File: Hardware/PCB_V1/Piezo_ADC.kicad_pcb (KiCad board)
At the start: 2 copper layers, 165 x 44.2 mm, 51 parts, among them J1 Conn_RJ45_Shielded_8p8c_RA_A-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, J2 Conn_2Pos_3.96mm_1Row_TH_JST_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, U1 IC_LDO_FIXED_3.3V_SC-70-5, U2 IC_TRANSCIEVER_RS485_DUPLEX_S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, U3 IC_ADC_SPI_12BIT_ADC121S021_S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, U4 IC_OPAMP_1MHz_TLV9001IDBVR_1A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, U5 IC_TRANSCIEVER_RS485_DUPLEX_S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

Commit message: Converted Altium PCB File to KiCAD
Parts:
- added TP6: TPAD6R, Footprints-lib:Single_TH_Pin_Header, F.Cu at (169.8, 105.4)
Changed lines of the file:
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@@
 		)
+	)
+	(footprint "Footprints-lib:Single_TH_Pin_Header"
+		(layer "F.Cu")
+		(at 169.782885 105.43992)
+		(property "Reference" "TP6"
+			(at 0 -2.54 0)
+			(unlocked yes)
+			(layer "F.SilkS")
+			(effects
+				(font
+					(size 1 1)
+					(thickness 0.1)
+				)
+			)
+		)
+		(property "Value" "TPAD6R"
+			(at 0 2.54 0)
+			(unlocked yes)
+			(layer "F.Fab")
+			(effects
+				(font
+					(size 1 1)
+					(thickness 0.15)
+				)
+			)
+		)
+		(property "Datasheet" ""
+			(at 0 0 0)
+			(unlocked yes)
+			(layer "F.Fab")
+			(hide yes)
+			(effects
+				(font
+					(size 1 1)
+					(thickness 0.15)
+				)
+			)
+		)
+		(property "Description" "0.6mm round"
+			(at 0 0 0)
+			(unlocked yes)
+			(layer "F.Fab")
+			(hide yes)
+			(effects
+				(font
+					(size 1 1)
+					(thickness 0.15)
+				)
+			)
+		)
+		(property "CASE/PACKAGE" ""
+			(at 0 0 0)
+			(unlocked yes)
+			(layer "F.Fab")
+			(hide yes)
+			(effects
+				(font
+					(size 1 1)
+					(thickness 0.15)
+				)
+			)
+		)
+		(property "ROHS COMPLIANT" ""
+			(at 0 0 0)
+			(unlocked yes)
+			(layer "F.Fab")
+			(hide yes)
+			(effects
+				(font
+					(size 1 1)
+					(thickness 0.15)
+				)
+			)
+		)
+		(property "MAX OPERATING TEMPERATURE" ""
+			(at 0 0 0)
+			(unlocked yes)
+			(layer "F.Fab")
+			(hide yes)
+			(effects
+				(font
+					(size 1 1)
+					(thickness 0.15)
+				)
+			)
+		)
+		(property "MIN OPERATING TEMPERATURE" ""
+			(at 0 0 0)
+			(unlocked yes)
+			(layer "F.Fab")
+			(hide yes)
+			(effects
+				(font
+					(size 1 1)
+					(thickness 0.15)
+				)
+			)
+		)
+		(property "MOUNTING TECHNOLOGY" ""
+			(at 0 0 0)
+			(unlocked yes)
+			(layer "F.Fab")
+			(hide yes)
+			(effects
+				(font
+					(size 1 1)
+					(thickness 0.15)
+				)
+			)
+		)
+		(property "PINS" "1"
+			(at 0 0 0)
+			(unlocked yes)
+			(layer "F.Fab")
+			(hide yes)
+			(effects
+				(font
+					(size 1 1)
+					(thickness 0.15)
+				)
+			)
+		)
+		(property ki_fp_filters "*TP06R*")
+		(sheetname "/")
+		(sheetfile "Piezo_ADC.kicad_sch")
+		(units
+			(unit
+				(name "A")
+				(pins "1")
+			)
+		)
+		(attr board_only)
+		(duplicate_pad_numbers_are_jumpers no)
+		(fp_circle
+			(center 0 0)
+			(end 1 0)
+			(stroke
+				(width 0.1)
+				(type solid)
+			)
+			(fill no)
+			(layer "F.SilkS")
+		)
+		(fp_rect
+			(start -1.52 -1.52)
+			(end 1.52 1.52)
+			(stroke
+				(width 0.05)
+				(type default)
+			)
+			(fill no)
+			(layer "F.CrtYd")
+		)
+		(fp_rect
+			(start -1.27 -1.27)
+			(end 1.27 1.27)
+			(stroke
+				(width 0.1)
+				(type default)
+			)
+			(fill no)
+			(layer "F.Fab")
+		)
+		(fp_text user "${REFERENCE}"
+			(at 0 3.81 0)
+			(unlocked yes)
+			(layer "F.Fab")
+			(effects
+				(font
+					(size 1 1)
+					(thickness 0.15)
+				)
+			)
+		)
+		(pad "1" thru_hole circle
+			(at 0 0)
+			(size 1.5 1.5)
+			(drill 0.8)
+			(layers "*.Cu" "*.Mask")
+			(remove_unused_layers no)
+			(net "/CS_SE")
+			(pinfunction "TP_1")
+			(pintype "passive")
+		)
+		(embedded_fonts no)
 	)
 	(footprint "Vault:RES_0402"

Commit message: Added 5015 test points to schematic
Waiting to get confirmation before I place them on the board.
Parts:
- added TP7: TPAD6R, TestPoint:TestPoint_Keystone_5015_Micro_Mini, F.Cu at (169.8, 108.9)
- added TP8: TPAD6R, TestPoint:TestPoint_Keystone_5015_Micro_Mini, F.Cu at (169.8, 115.2)
- TP6: footprint Footprints-lib:Single_TH_Pin_Header -> TestPoint:TestPoint_Keystone_5015_Micro_Mini
- moved TP6 2.75 mm to (169.8, 102.7)

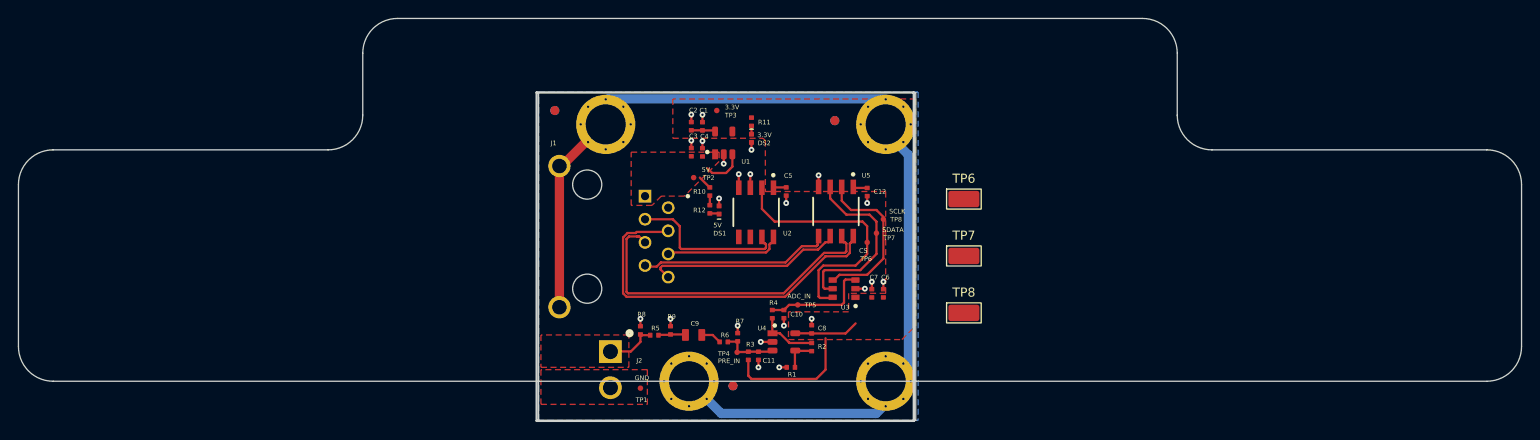
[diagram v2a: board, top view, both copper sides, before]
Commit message: PCB Updates
- Added keystone 5001 test points
- Added Schottky diodes
- reworked the board layout to make room for TPs and additional components.
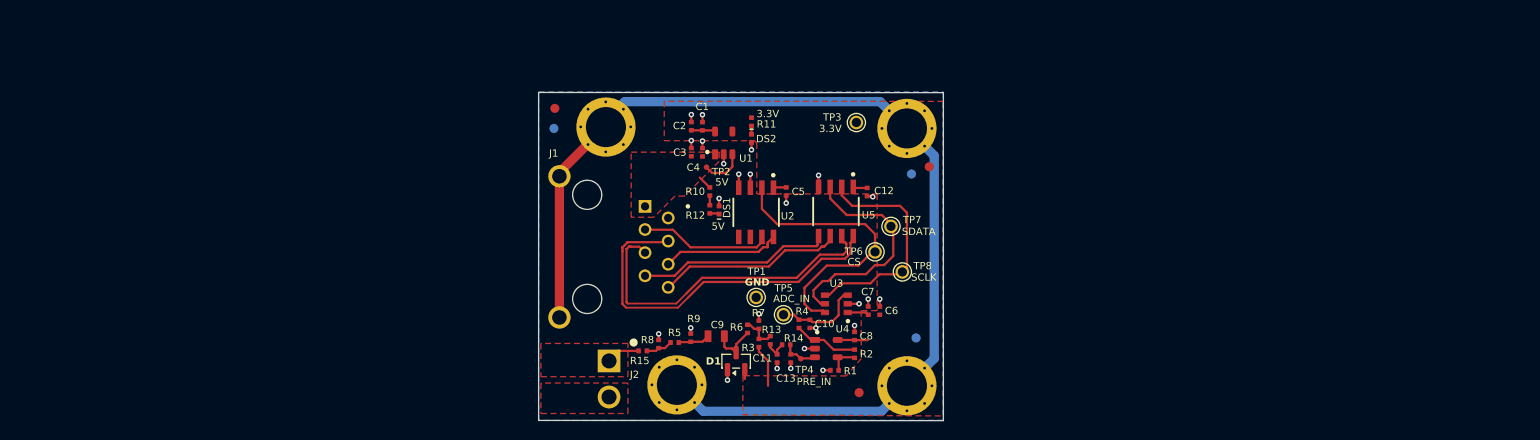
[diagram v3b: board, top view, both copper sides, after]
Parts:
- removed the TP6 at (169.8, 102.7)
- removed the TP6 at (159.2, 107.5)
- removed the TP7 at (169.8, 108.9)
- removed the TP7 at (160.2, 106.4)
- removed the TP8 at (169.8, 115.2)
- removed the TP8 at (160.9, 104.9)
- added C13: Cap_0.1uF_10%_16V_0402, Piezo_Footprints:CAP_0402_0.6mm_Height, F.Cu at (150.8, 120.2)
- added D1: BAT54S, Package_TO_SOT_SMD:SOT-23, F.Cu at (144.8, 120.5)
- added R13: Res_0R0_1%_63mW_0402, Piezo_Footprints:RES_0402, F.Cu at (148.5, 118.2)
- added R14: Res_0R0_1%_63mW_0402, Piezo_Footprints:RES_0402, F.Cu at (150.3, 118.7)
- added R15: Res_0R0_1%_63mW_0402, Piezo_Footprints:RES_0402, F.Cu at (134.5, 119.4)
- added TP6: TPAD6R, Piezo_Footprints:Keystone 5001 TP, F.Cu at (160.0, 108.5)
- added TP7: TPAD6R, Piezo_Footprints:Keystone 5001 TP, F.Cu at (161.8, 105.7)
- added TP8: TPAD6R, Piezo_Footprints:Keystone 5001 TP, F.Cu at (163.0, 110.7)
- C1, C10, C11, C12, C2, C3, C4, C5, C6, C7, C8: footprint Vault:CAP_0402_0.6mm_Height -> Piezo_Footprints:CAP_0402_0.6mm_Height
- C9: footprint Vault:CAP_0805_1.45mm_Height -> Piezo_Footprints:CAP_0805_1.45mm_Height
- DS1, DS2: footprint Vault:LED_0402_Green_KA -> Piezo_Footprints:LED_0402_Green_KA
- FD1, FD3, FD5, FD6: footprint Vault:FID1X2R -> Piezo_Footprints:FID1X2R
- FD2: footprint Vault:FID1X2R -> Piezo_Footprints:FID1X2R; moved to B.Cu
- FD4: footprint Vault:FID1X2R -> Piezo_Footprints:FID1X2R; moved to F.Cu
- J1: footprint Vault:A-2004-2-4-LPS-N-R -> Piezo_Footprints:A-2004-2-4-LPS-N-R
- J2: footprint Vault:JST_B2PS-VH-FP -> Piezo_Footprints:JST_B2PS-VH-FP
- MP1, MP2, MP3, MP4: footprint Vault:9774020960 -> Piezo_Footprints:9774020960
- R1, R10, R11, R12, R2, R3, R4, R5, R6, R7, R8, R9: footprint Vault:RES_0402 -> Piezo_Footprints:RES_0402
- TP1, TP3, TP5: footprint Vault:TP06R -> Piezo_Footprints:Keystone 5001 TP
- TP2, TP4: footprint Vault:TP06R -> Piezo_Footprints:TP06R
- U1, U4: footprint Vault:SOT23-5 -> Piezo_Footprints:SOT23-5
- U2, U5: footprint Vault:SOIC-8 -> Piezo_Footprints:SOIC-8
- U3: footprint Vault:SOT-23-6 -> Piezo_Footprints:SOT-23-6
- moved FD4 45.6 mm to (158.3, 123.9), turned to 0 degrees
- moved FD3 32.3 mm to (166.0, 99.1), turned to 0 degrees
- moved FD5 30.8 mm to (124.8, 94.9), turned to 180 degrees
- moved FD6 30.4 mm to (164.0, 99.9), turned to 180 degrees
- moved FD2 25.5 mm to (164.5, 117.9), turned to 180 degrees
- moved TP1 16.1 mm to (147.0, 113.5)
- moved TP3 15.4 mm to (158.0, 94.3), turned to 0 degrees
- moved TP4 7.03 mm to (151.9, 120.2)
- moved R1 4.81 mm to (155.6, 121.5)
- moved C8 4.77 mm to (157.8, 117.7)
- moved R2 4.77 mm to (157.8, 119.7)
- moved U4 4.71 mm to (154.7, 119.1)
- moved R4 3.12 mm to (151.7, 116.4)
- moved C10 3.05 mm to (152.9, 116.4)
- moved R6 2.98 mm to (146.0, 116.9), turned to 90 degrees
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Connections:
- net ADC_IN renamed /ADC_IN
- net CS_DIFF_N renamed /CS_DIFF_N
- net CS_DIFF_P renamed /CS_DIFF_P
- net NetC9_1 renamed Net-(C9-Pad1)
- net NetC9_2 renamed Net-(D1-COM)
- net NetDS1_1 renamed Net-(DS1-A)
- net NetDS2_1 renamed Net-(DS2-A)
- net NetR10_1 renamed Net-(R10-Pad1)
- net NetR1_1 renamed Net-(U4--IN)
- net NetR2_2 renamed Net-(U4-OUT)
- net SCLK_DIFF_N renamed /SCLK_DIFF_N
- net SCLK_DIFF_P renamed /SCLK_DIFF_P
- net SDATA_DIFF_N renamed /SDATA_DIFF_N
- net SDATA_DIFF_P renamed /SDATA_DIFF_P
- C11 pad 1: PREAMP_IN -> Net-(C11-Pad1)
- J2 pad 1: PIEZO_IN -> /PIEZO_IN
- R3 pad 1: PREAMP_IN -> Net-(R13-Pad1)
- R5 pad 1: PIEZO_IN -> Net-(R15-Pad2)
- R6 pad 2: PREAMP_IN -> Net-(R13-Pad1)
- R7 pad 2: PREAMP_IN -> Net-(R13-Pad1)
- R8 pad 2: PIEZO_IN -> Net-(R15-Pad2)
- TP4 pad 1: PREAMP_IN -> /PREAMP_IN
- U1 pad 4: (no net) -> unconnected-(U1-NC-Pad4)
- U2 pad 2: CS_SE -> /CS_SE
- U2 pad 5: (no net) -> unconnected-(U2-Y-Pad5)
- U2 pad 6: (no net) -> unconnected-(U2-Z-Pad6)
- U3 pad 4: SCLK_SE -> /SCLK_SE
- U3 pad 5: SDATA_SE -> /SDATA_SE
- U3 pad 6: CS_SE -> /CS_SE
- U4 pad 3: PREAMP_IN -> /PREAMP_IN
- U5 pad 2: SCLK_SE -> /SCLK_SE
- U5 pad 3: SDATA_SE -> /SDATA_SE
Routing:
- net /CS_SE: track 0.00 -> 31.4 mm
- net CS_SE: track 28.2 -> 0.00 mm
- net /SDATA_SE: track 0.00 -> 25.3 mm
- net /SCLK_SE: track 0.00 -> 25.1 mm
- net SDATA_SE: track 20.4 -> 0.00 mm
- net SCLK_SE: track 17.5 -> 0.00 mm
- net 3V3: track 27.0 -> 16.5 mm
- net PREAMP_IN: track 6.30 -> 0.00 mm
- net CH_GND: track 114.1 -> 120.3 mm
- net PIEZO_IN: track 5.67 -> 0.00 mm
- net Net-(R13-Pad1): track 0.00 -> 3.91 mm
- net /PREAMP_IN: track 0.00 -> 3.75 mm
- net /PIEZO_IN: track 0.00 -> 3.73 mm
- net Net-(D1-COM): track 2.28 -> 5.91 mm
- net Net-(R15-Pad2): track 0.00 -> 2.98 mm
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- added copper zone on F.Cu, net /PIEZO_IN
- removed copper zone on F.Cu, net PIEZO_IN
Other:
- board size 165 x 44.2 mm -> 44.4 x 36 mm

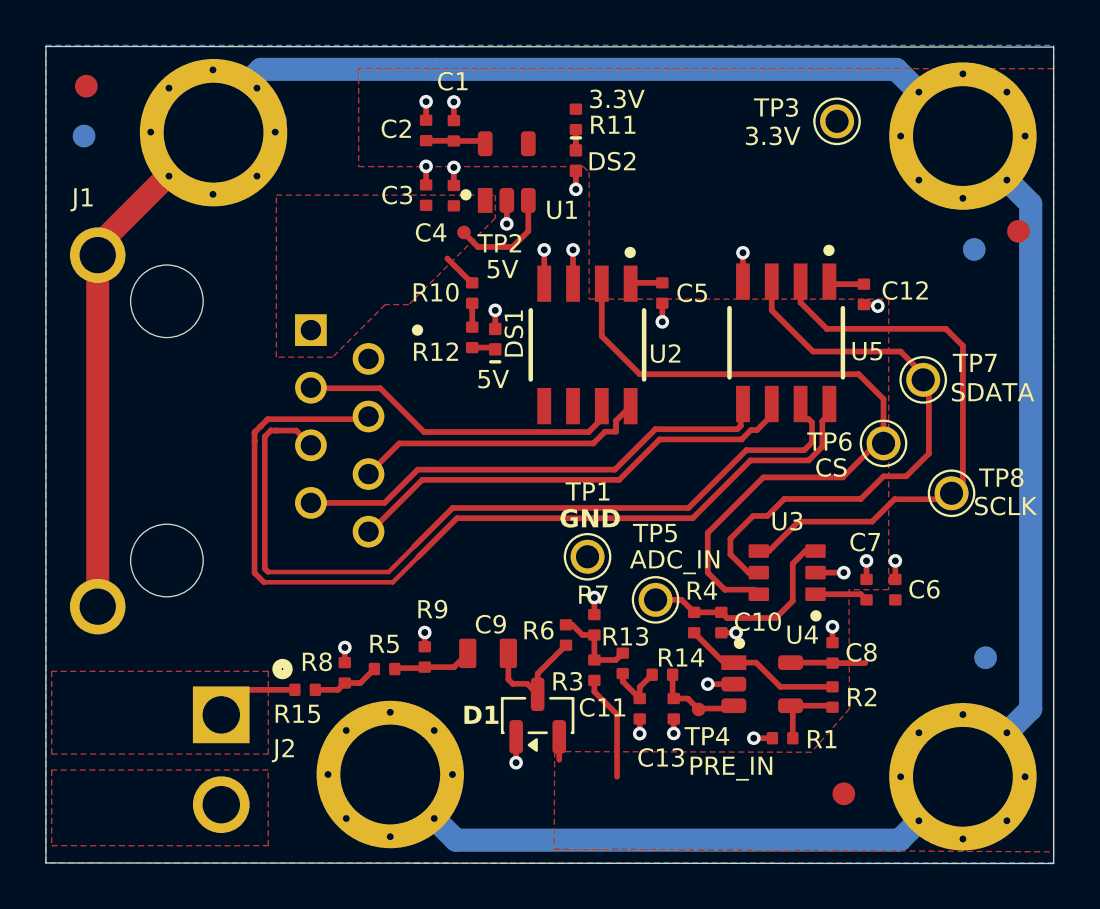
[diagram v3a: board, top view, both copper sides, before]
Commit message: Moved fiducial markers, removed section of solder mask from risers we are no longer using.
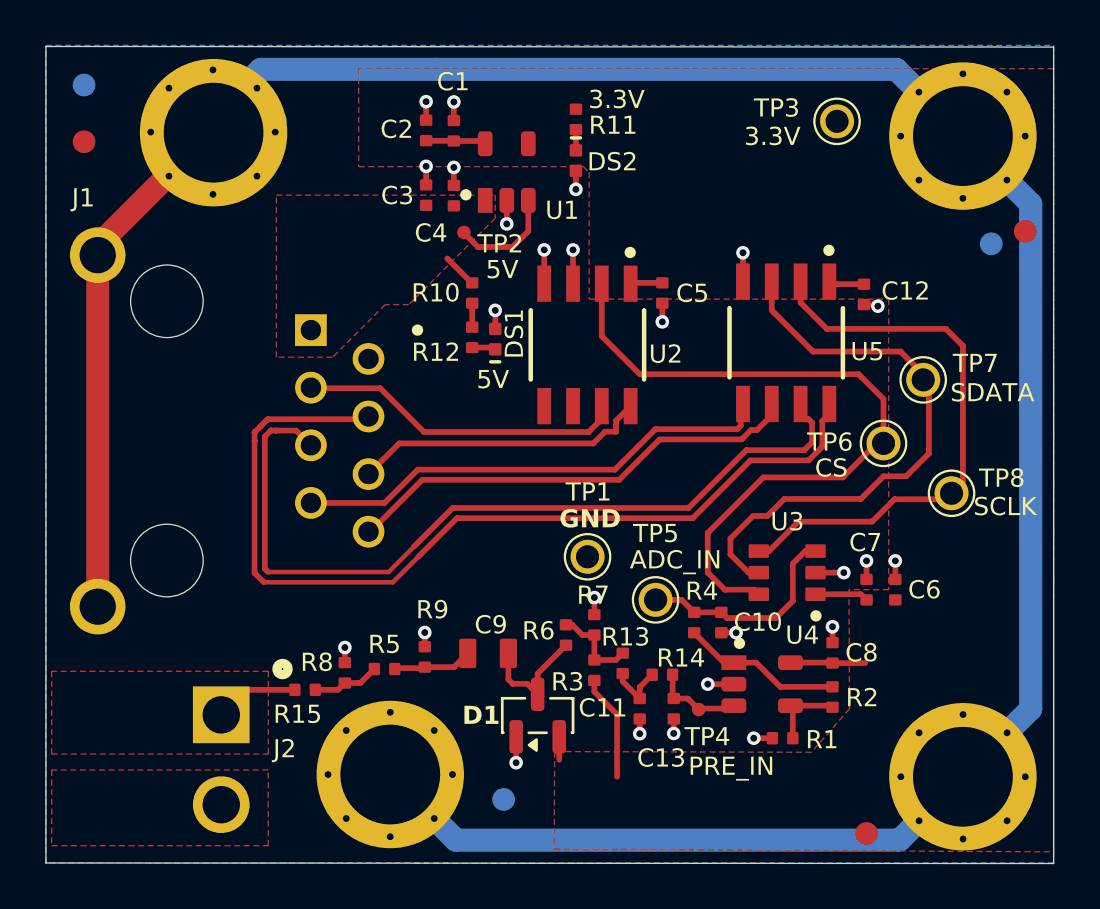
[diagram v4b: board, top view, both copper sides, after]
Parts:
- C11: value Cap_0.1uF_10%_16V_0402 -> Cap_2.05nF_10%_16V_0402
- C13: value Cap_0.1uF_10%_16V_0402 -> Cap_1nF_10%_16V_0402
- R13, R14: value Res_0R0_1%_63mW_0402 -> Res_2.26kR0_1%_63mW_0402
- moved FD2 22.2 mm to (143.3, 124.2)
- moved FD1 2.45 mm to (124.8, 95.2)
- moved FD5 2.25 mm to (124.8, 92.7)
- moved FD4 2.02 mm to (159.3, 125.7)
- moved FD6 0.79 mm to (164.8, 99.7)
- moved FD3 0.30 mm to (166.3, 99.1)
